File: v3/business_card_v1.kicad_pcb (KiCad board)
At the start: 16 copper layers, 89 x 51 mm, 78 parts, among them IC1 ATTINY24_44_84-SSU, SW1 SPST_TACT-KMR2

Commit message: add the final touches to the Pcb
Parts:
- removed C1: 0.1uF, business_card_v1:C0805
- removed IC1: ATTINY24_44_84-SSU, business_card_v1:SOIC14
- removed R2, R3, R4, R5, R6, R7, R8, R9: 150, business_card_v1:R0805
- removed TP1, TP2, TP3, TP4, TP5, TP6: TEST-POINTPOGO_PTH, business_card_v1:1X01_NO_SILK
- removed U$1: , business_card_v1:OSHWLOGO_TOP_0.2
- removed U$2, U$3: , business_card_v1:OSHWLOGO_TOL_0.2
- added C2: 1u, Capacitor_SMD:C_0603_1608Metric, F.Cu at (126.4, 115.6)
- added C3: 1u, Capacitor_SMD:C_0603_1608Metric, F.Cu at (128.3, 115.6)
- added J1: Conn_01x05_Male, Connector_PinHeader_2.54mm:PinHeader_1x05_P2.54mm_Vertical, B.Cu at (132.1, 116.5)
- added J2: Conn_01x01_Male, Connector_PinSocket_2.54mm:PinSocket_1x01_P2.54mm_Vertical, B.Cu at (122.5, 116.5)
- added R10: 10K, Resistor_SMD:R_0603_1608Metric, F.Cu at (137.8, 117.5)
- added REF**: OSHW-Symbol_6.7x6mm_SilkScreen, Symbol:OSHW-Symbol_6.7x6mm_SilkScreen, B.Cu at (141.2, 86.6)
- added REF**: KiCad-Logo_6mm_SilkScreen, Symbol:KiCad-Logo_6mm_SilkScreen, B.Cu at (114.8, 86.6)
- added RN1: R_Pack04, Resistor_SMD:R_Array_Convex_4x1206, F.Cu at (146.7, 118.1)
- added RN2: R_Pack04, Resistor_SMD:R_Array_Convex_4x1206, F.Cu at (146.7, 125.7)
- added U1: MIC5504-3.3YM5, Package_TO_SOT_SMD:SOT-23-5, F.Cu at (127.0, 120.0)
- added U2: STM32G030F6P6, Package_SO:TSSOP-20_4.4x6.5mm_P0.65mm, F.Cu at (138.7, 124.7)
- R1: footprint business_card_v1:R0805 -> Resistor_SMD:R_0603_1608Metric
- SW1: value SPST_TACT-KMR2 -> SW_SPST; footprint business_card_v1:KMR2 -> Button_Switch_SMD:SW_Push_1P1T_NO_CK_KMR2
- moved SW1 8.63 mm to (141.6, 116.2), turned to 90 degrees
- moved R1 2.59 mm to (135.9, 117.5)
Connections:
- JP1 pad 5V: UCC -> +5V
- JP1 pad USB_M: Net-(JP1-PadUSB_M) -> (no net)
- JP1 pad USB_P: Net-(JP1-PadUSB_P) -> (no net)
- R1 pad 1: /RESET -> SWDCLK-BOOT0
- R1 pad 2: UCC -> GND
- SW1 pad 1: Net-(SW1-Pad1) -> RST
- SW1 pad 2: Net-(SW1-Pad2) -> GND
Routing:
- net /PIN7: track 60.6 -> 0.00 mm
- net /MOSI: track 57.1 -> 0.00 mm, vias 1 -> 0
- net /MISO: track 52.7 -> 0.00 mm, vias 1 -> 0
- net /SCK: track 50.4 -> 0.00 mm, vias 1 -> 0
- net Net-(LED1-PadC): track 91.5 -> 134.2 mm
- net Net-(LED10-PadC): track 99.1 -> 136.1 mm
- net Net-(LED14-PadA): track 104.2 -> 135.6 mm
- net Net-(LED13-PadA): track 109.3 -> 135.6 mm
- net /PIN3: track 24.2 -> 0.00 mm
- net RST: track 0.00 -> 22.1 mm, vias 0 -> 2
- net +5V: track 0.00 -> 19.9 mm
- net Net-(LED12-PadA): track 109.3 -> 128.5 mm
- net PINE: track 0.00 -> 18.7 mm
- net /PIN2: track 18.6 -> 0.00 mm
- net SWDCLK-BOOT0: track 0.00 -> 17.2 mm, vias 0 -> 2
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- added copper zone on F.Cu, net +3V3
- removed copper zone on F.Cu, net UCC
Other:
- board text added: "3.3V-REF"
- board text added: "5v-SUP"
- board text added: "B.E. Electrical Engineering & B.Sc. Computer Science Website: kevin.lutzer.ca Email: kevin@lutzer.ca Github: github.com/kevinlutzer LinkedIn: linkedin.com/in/kevin-lutzer"
- board text added: "GND"
- board text added: "Open Source"
- board text added: "RST"
- board text added: "SWDCLK"
- board text added: "SWDIO"
- board text added: "designed with"
- board text added: "v3"
- board text removed: "B.E. Electrical Engineering & B.Sc. Computer Science"
- board text removed: "Website: kevin.lutzer.ca Email: kevin@lutzer.ca Github: github.com/kevinlutzer LinkedIn: linkedin.com/in/kevin-lutzer"
- board text removed: "v2.1"

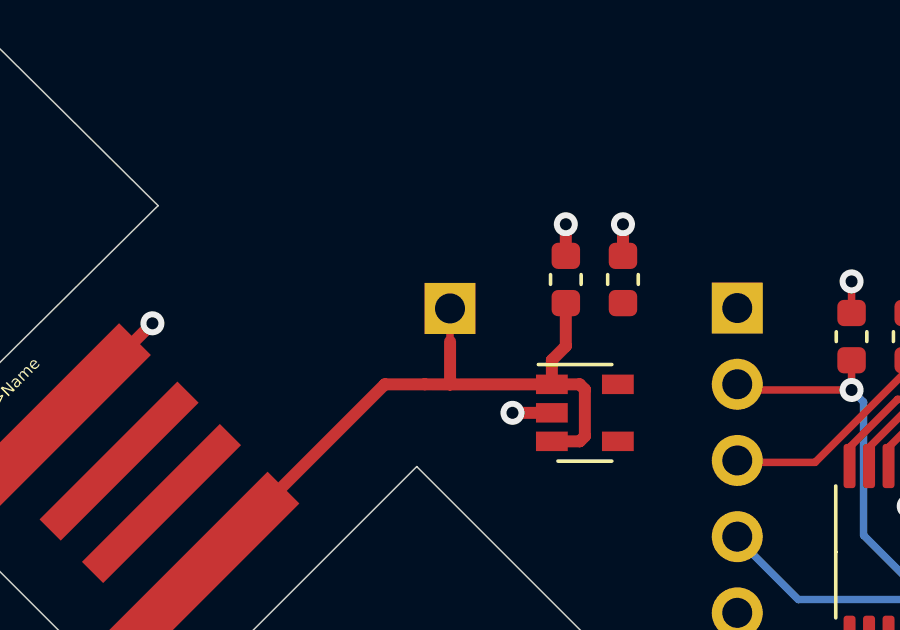
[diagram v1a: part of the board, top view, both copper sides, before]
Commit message: add dimensions
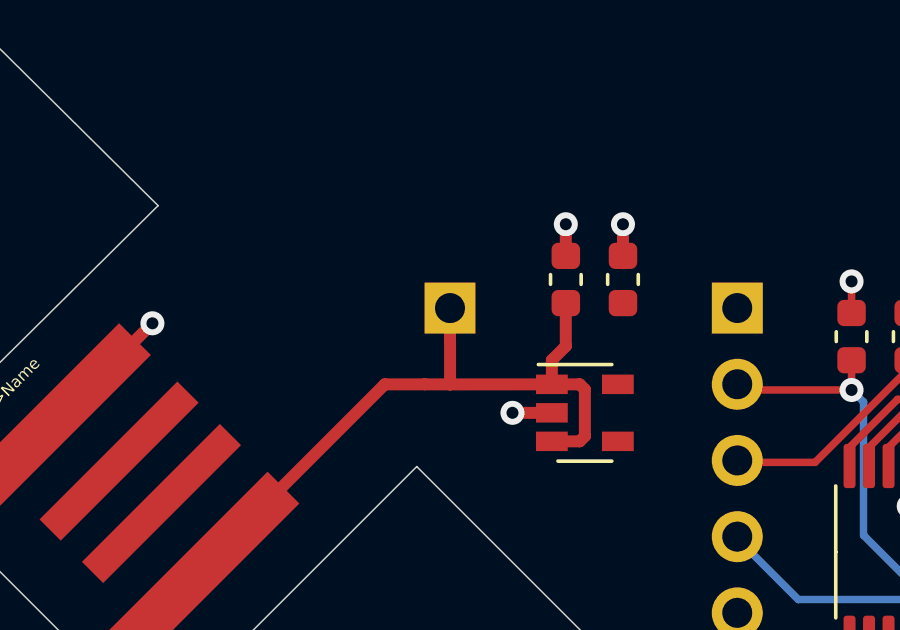
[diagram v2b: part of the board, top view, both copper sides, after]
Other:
- board text added: "open source"
- board text removed: "Open Source"
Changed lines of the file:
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@@
   (general
     (thickness 1.6)
-    (drawings 243)
+    (drawings 246)
     (tracks 424)
     (zones 0)
@@
     (mod_text_size 1 1)
     (mod_text_width 0.15)
-    (pad_size 1.524 1.524)
-    (pad_drill 0.762)
+    (pad_size 1.7 1.7)
+    (pad_drill 1)
     (pad_to_mask_clearance 0.051)
     (solder_mask_min_width 0.25)
@@
     (fp_line (start 0.635 1.27) (end 1.27 0.635) (layer B.Fab) (width 0.1))
     (fp_line (start -1.27 1.27) (end 0.635 1.27) (layer B.Fab) (width 0.1))
-    (pad 1 thru_hole rect (at 0 0) (size 1.7 1.7) (drill 1) (layers *.Cu *.Mask)
+    (pad 1 thru_hole rect (at 0 -0.0127) (size 1.7 1.7) (drill 1) (layers *.Cu *.Mask)
       (net 10 +5V))
     (model ${KISYS3DMOD}/Connector_PinSocket_2.54mm.3dshapes/PinSocket_1x01_P2.54mm_Vertical.wrl
@@
       (net 9 "Net-(LED1-PadC)") (solder_mask_margin 0.1016))
   )
+  (dimension 9.575808 (width 0.15) (layer Cmts.User)
+    (gr_text "9.576 mm" (at 127.321056 138.361681 0.07598905294) (layer Cmts.User)
+      (effects (font (size 1 1) (thickness 0.15)))
+    )
+    (feature1 (pts (xy 132.08 116.5225) (xy 132.10801 137.641752)))
+    (feature2 (pts (xy 122.5042 116.5352) (xy 122.53221 137.654452)))
+    (crossbar (pts (xy 122.531432 137.068032) (xy 132.107232 137.055332)))
+    (arrow1a (pts (xy 132.107232 137.055332) (xy 130.981507 137.643246)))
+    (arrow1b (pts (xy 132.107232 137.055332) (xy 130.979951 136.470406)))
+    (arrow2a (pts (xy 122.531432 137.068032) (xy 123.658713 137.652958)))
+    (arrow2b (pts (xy 122.531432 137.068032) (xy 123.657157 136.480118)))
+  )
+  (dimension 13.9827 (width 0.15) (layer Cmts.User)
+    (gr_text "13.983 mm" (at 92.426 123.51385 270) (layer Cmts.User)
+      (effects (font (size 1 1) (thickness 0.15)))
+    )
+    (feature1 (pts (xy 132.08 130.5052) (xy 93.139579 130.5052)))
+    (feature2 (pts (xy 132.08 116.5225) (xy 93.139579 116.5225)))
+    (crossbar (pts (xy 93.726 116.5225) (xy 93.726 130.5052)))
+    (arrow1a (pts (xy 93.726 130.5052) (xy 93.139579 129.378696)))
+    (arrow1b (pts (xy 93.726 130.5052) (xy 94.312421 129.378696)))
+    (arrow2a (pts (xy 93.726 116.5225) (xy 93.139579 117.649004)))
+    (arrow2b (pts (xy 93.726 116.5225) (xy 94.312421 117.649004)))
+  )
+  (dimension 70.485 (width 0.15) (layer Cmts.User)
+    (gr_text "70.485 mm" (at 157.7467 143.8194) (layer Cmts.User)
+      (effects (font (size 1 1) (thickness 0.15)))
+    )
+    (feature1 (pts (xy 192.9892 116.5352) (xy 192.9892 143.105821)))
+    (feature2 (pts (xy 122.5042 116.5352) (xy 122.5042 143.105821)))
+    (crossbar (pts (xy 122.5042 142.5194) (xy 192.9892 142.5194)))
+    (arrow1a (pts (xy 192.9892 142.5194) (xy 191.862696 143.105821)))
+    (arrow1b (pts (xy 192.9892 142.5194) (xy 191.862696 141.932979)))
+    (arrow2a (pts (xy 122.5042 142.5194) (xy 123.630704 143.105821)))
+    (arrow2b (pts (xy 122.5042 142.5194) (xy 123.630704 141.932979)))
+  )
   (gr_text 5v-SUP (at 127 116.84) (layer B.SilkS)
     (effects (font (size 1 1) (thickness 0.14224)) (justify mirror))
@@
     (effects (font (size 1 1) (thickness 0.14224)) (justify mirror))
   )
-  (gr_text "Open Source" (at 137.668 82.296) (layer B.SilkS)
+  (gr_text "open source" (at 137.668 82.296) (layer B.SilkS)
     (effects (font (size 1.5 1.5) (thickness 0.14224)) (justify mirror))
   )
@@
   (segment (start 120.33 119.065) (end 116.84 122.555) (width 0.4) (layer Top) (net 10))
   (segment (start 122.50674 117.63774) (end 122.50674 119.06758) (width 0.4) (layer Top) (net 10))
-  (segment (start 122.5042 116.5352) (end 122.5042 117.6352) (width 0.25) (layer Top) (net 10))
+  (segment (start 122.5042 116.5352) (end 122.5042 117.6352) (width 0.4) (layer Top) (net 10))
   (segment (start 122.50674 119.06758) (end 125.9 119.065) (width 0.4) (layer Top) (net 10))
   (segment (start 122.5042 117.6352) (end 122.50674 117.63774) (width 0.25) (layer Top) (net 10))
